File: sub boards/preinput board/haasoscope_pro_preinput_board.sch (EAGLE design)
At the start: 55 parts, among them J4 8pin, K1 G6K-2F-RF-T-TR03_DC5, K2 G6K-2F-RF-T-TR03_DC5, K3 TLP3475R_TP,F, K5 G6K-2F-RF-T-TR03_DC5, Q1 S8050, Q2 S8050, Q3 S8050

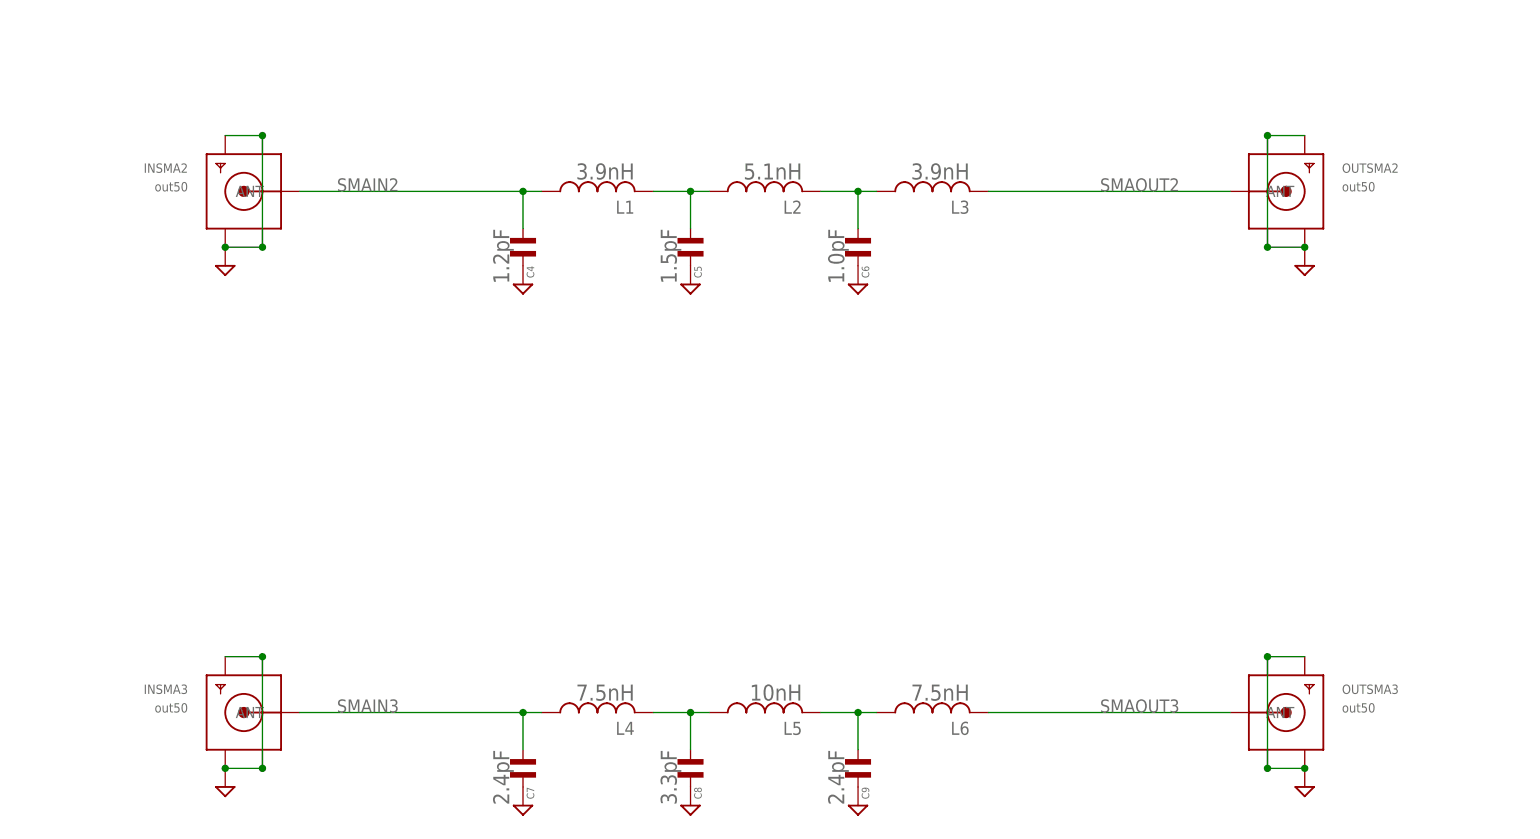
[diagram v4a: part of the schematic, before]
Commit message: update filter values, 5th order
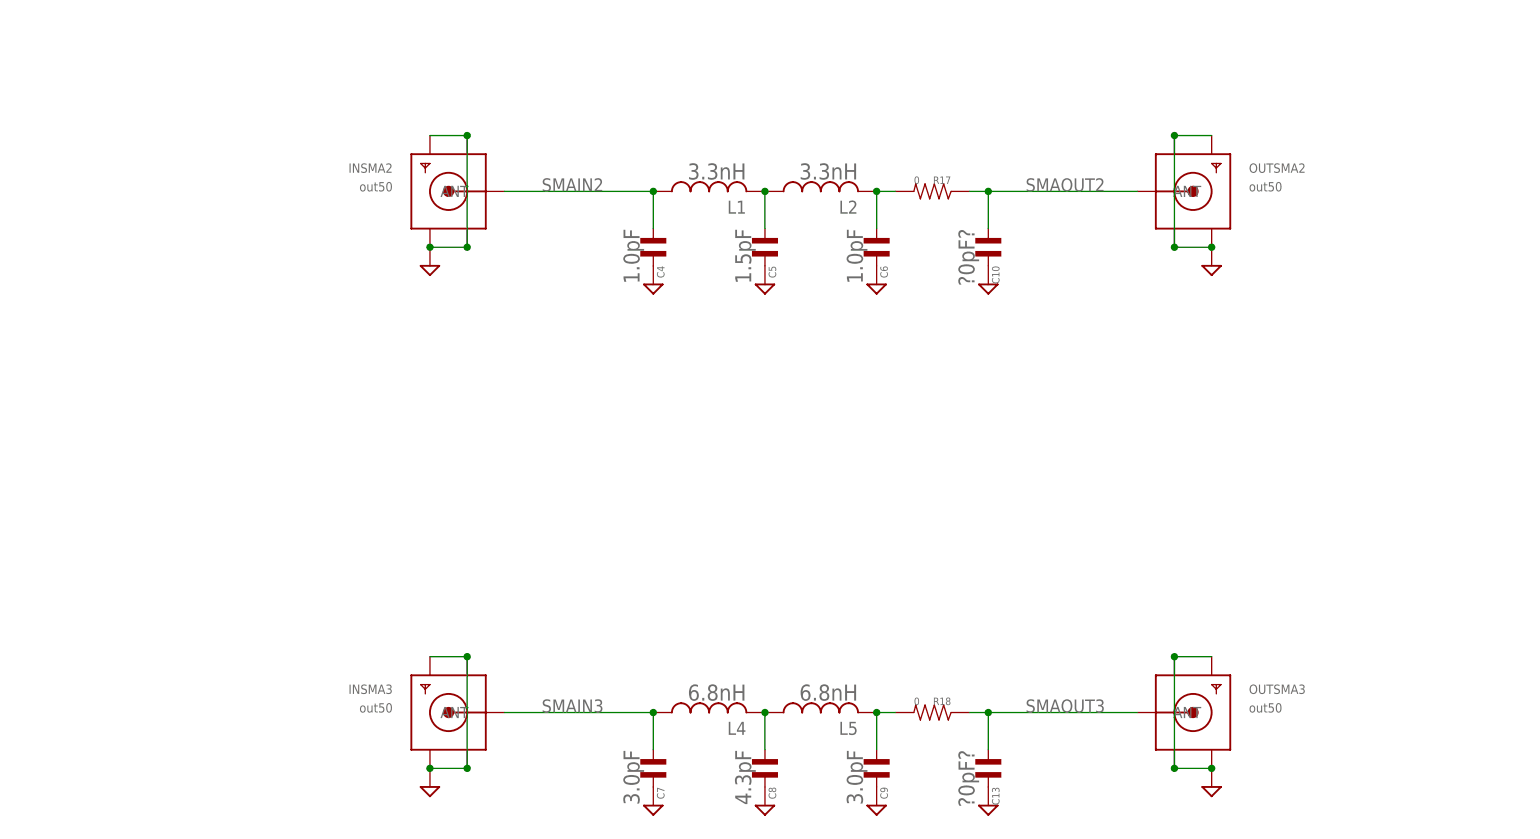
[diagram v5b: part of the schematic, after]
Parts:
- removed L3: 3.9nH, Nordic_nRF:INDUCTOR_0402_N
- removed L6: 7.5nH, Nordic_nRF:INDUCTOR_0402_N
- added C10, C13: ?0pF?, MF_Passives:CAPACITOR_NP_0402
- added R17, R18: 0, MF_Passives:RESISTOR_0402
- C4: value 1.2pF -> 1.0pF
- C7, C9: value 2.4pF -> 3.0pF
- C8: value 3.3pF -> 4.3pF
- L1: value 3.9nH -> 3.3nH
- L2: value 5.1nH -> 3.3nH
- L4: value 7.5nH -> 6.8nH
- L5: value 10nH -> 6.8nH
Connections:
- net GND: now also C10.P$2, C13.P$2
- net N$11: now also R18.P$2; no longer L6.1
- net N$9: now also R17.P$2; no longer L3.1
- net SMAOUT2: now also C10.P$1, R17.P$1; no longer L3.2
- net SMAOUT3: now also C13.P$1, R18.P$1; no longer L6.2
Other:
- note added: "Chebyshev Lowpass Filter 1.4 GHz 5th order 50 Ohm 0.5dB ripple"
- note added: "Chebyshev Lowpass Filter 2.8 GHz 5th order 50 Ohm 0.5dB ripple"
- note added: "In case we try 7th order"
- note removed: "Chebyshev Lowpass Filter 1.25 GHz 6th order 50 Ohm 0.5dB ripple Pi: 4.394pF 7.944nH 6.637pF 8.363nH 6.305pF 5.536nH"
- note removed: "Chebyshev Lowpass Filter 2.5 GHz 6th order 50 Ohm 0.5dB ripple Pi: 2.197pF 3.972nH 3.319pF 4.181nH 3.152pF 2.768nH"
- moved on the sheet: C4, C5, C6, C7, C8, C9, INSMA2, INSMA3, L1, L2, L4, L5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
